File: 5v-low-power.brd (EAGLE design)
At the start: 68.6 x 40.3 mm, 34 parts, among them J1 Bypass, J2 En, J3 12v, J4 5V Out, J5 LED EN, J6 POWERPOLE_POWER10AWG, J7 POWERPOLE_POWER10AWG, Q1 SI4532ADY, U1 LT1934ES6TRMPBF

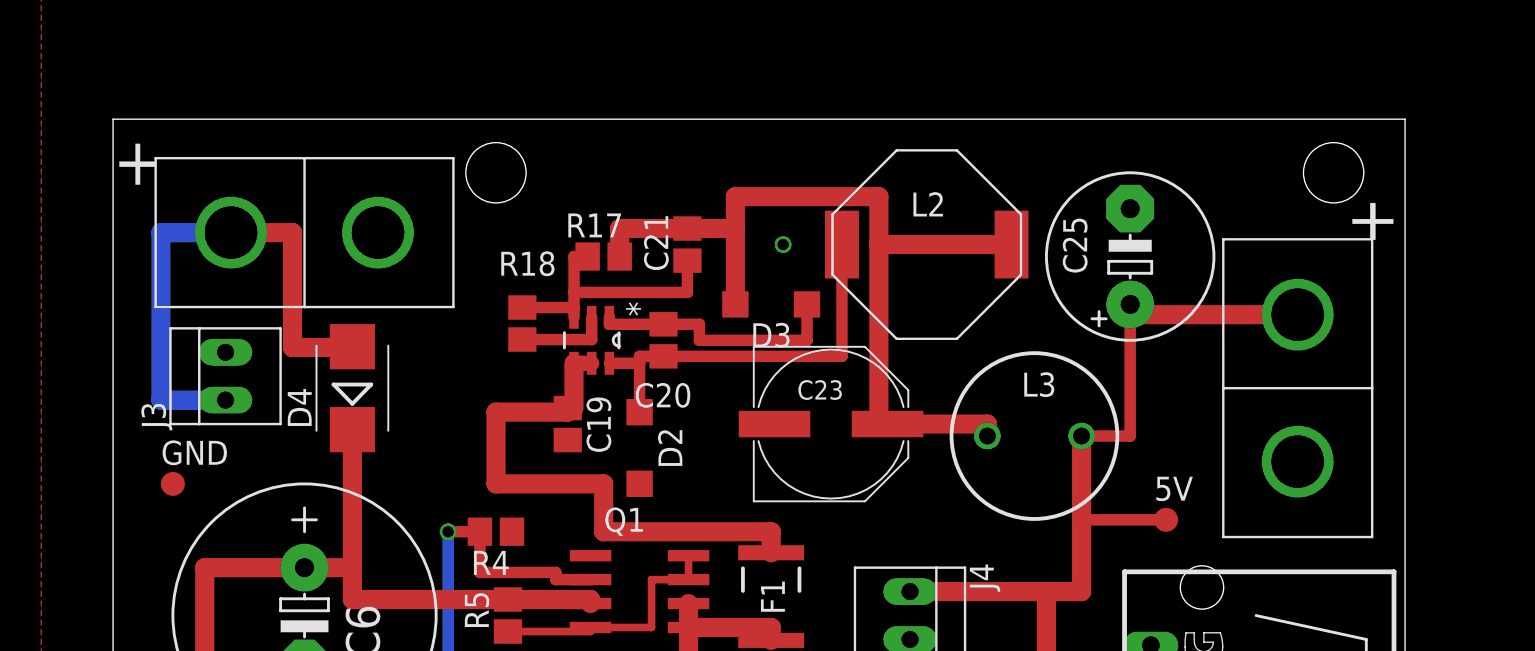
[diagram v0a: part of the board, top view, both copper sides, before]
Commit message: changed to correct powerpole version added current rating onto docu layer
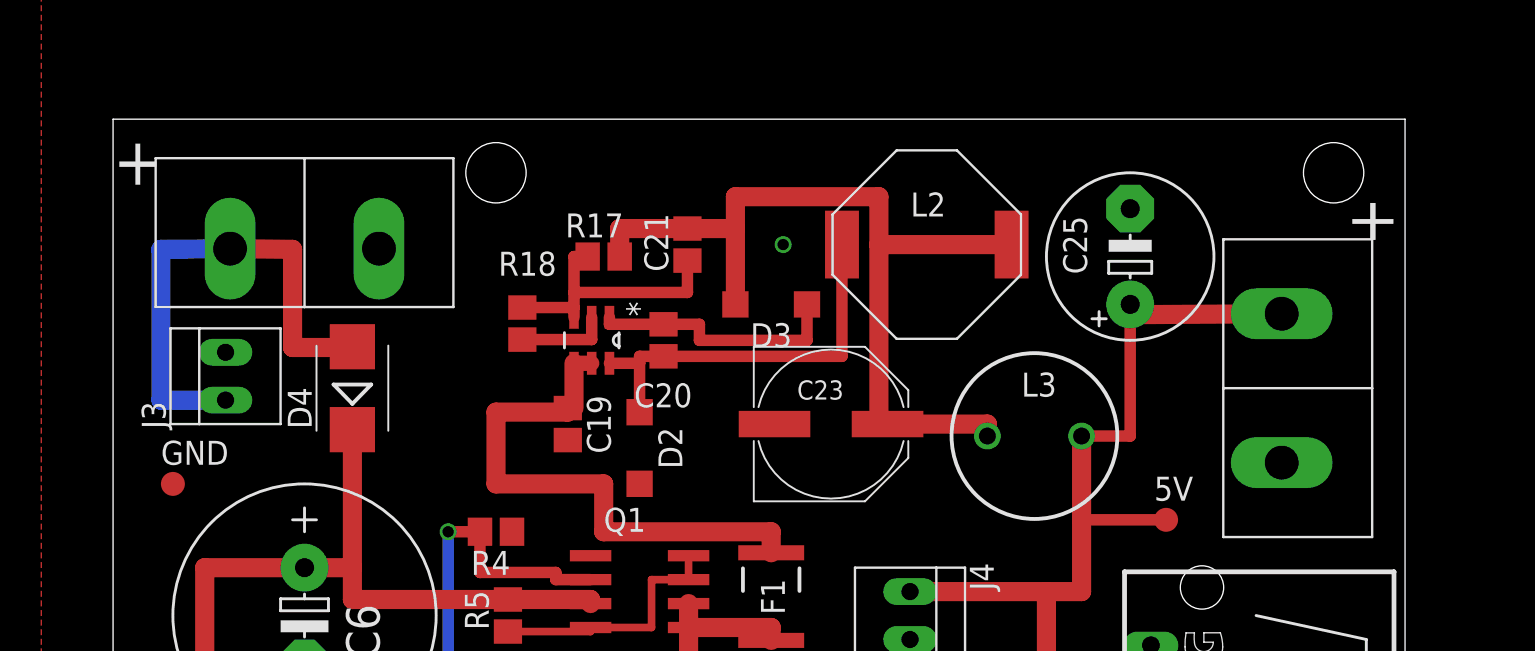
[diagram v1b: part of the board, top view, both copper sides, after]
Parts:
- J6, J7: value POWERPOLE_POWER10AWG -> POWERPOLE_POWER25A; device powerpoles:POWERPOLE_PAIR_10AWG -> powerpoles:POWERPOLE_PAIR_25A
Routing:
- net N$3: track 28.6 -> 26.8 mm
- net 5V: track 59.0 -> 58.1 mm
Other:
- board text added: "250mA"
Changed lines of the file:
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@@
 <text x="2.54" y="6.35" size="1.778" layer="51" rot="R90">V0.1</text>
 <text x="2.54" y="14.605" size="1.778" layer="51" rot="R90">PJB</text>
+<text x="53.975" y="38.1" size="1.778" layer="51">250mA</text>
 </plain>
 <attributes>
@@
 </element>
 <element name="J3" library="farnell-parts" package="2-MOLEX" value="12v" x="6.35" y="26.67" rot="R270"/>
-<element name="J6" library="powerpoles" package="POWERPOLE_PAIR_10AWG" value="POWERPOLE_POWER10AWG" x="62.865" y="26.035" rot="R270"/>
-<element name="J7" library="powerpoles" package="POWERPOLE_PAIR_10AWG" value="POWERPOLE_POWER10AWG" x="10.16" y="34.29"/>
+<element name="J6" library="powerpoles" package="POWERPOLE_PAIR_25A" value="POWERPOLE_POWER25A" x="62.865" y="26.035" rot="R270"/>
+<element name="J7" library="powerpoles" package="POWERPOLE_PAIR_25A" value="POWERPOLE_POWER25A" x="10.16" y="34.29"/>
 </elements>
 <signals>
@@
 <wire x1="51.395" y1="23.495" x2="53.975" y2="23.495" width="0.6096" layer="1"/>
 <wire x1="53.975" y1="23.495" x2="53.975" y2="30.48" width="0.6096" layer="1"/>
-<wire x1="62.865" y1="29.935" x2="53.975" y2="29.935" width="1.016" layer="1"/>
+<wire x1="62.015" y1="29.985" x2="53.975" y2="29.935" width="1.016" layer="1"/>
 <wire x1="53.975" y1="29.935" x2="53.975" y2="30.48" width="1.016" layer="1"/>
 <wire x1="42.291" y1="15.24" x2="49.53" y2="15.24" width="1.016" layer="1"/>
@@
 <contactref element="J7" pad="RED"/>
 <wire x1="5.969" y1="25.4" x2="2.54" y2="25.4" width="1.016" layer="16"/>
-<wire x1="2.54" y1="25.4" x2="2.54" y2="34.29" width="1.016" layer="16"/>
-<wire x1="2.54" y1="34.29" x2="6.26" y2="34.29" width="1.016" layer="16"/>
-<wire x1="6.26" y1="34.29" x2="9.525" y2="34.29" width="1.016" layer="1"/>
-<wire x1="9.525" y1="34.29" x2="9.525" y2="28.194" width="1.016" layer="1"/>
+<wire x1="2.54" y1="25.4" x2="2.54" y2="33.401" width="1.016" layer="16"/>
+<wire x1="2.54" y1="33.401" x2="6.21" y2="33.44" width="1.016" layer="16"/>
+<wire x1="6.21" y1="33.44" x2="9.525" y2="33.401" width="1.016" layer="1"/>
+<wire x1="9.525" y1="33.401" x2="9.525" y2="28.194" width="1.016" layer="1"/>
 <wire x1="9.525" y1="28.194" x2="12.7" y2="28.194" width="1.016" layer="1"/>
 <wire x1="12.7" y1="28.194" x2="12.7" y2="28.235" width="1.016" layer="1"/>

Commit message: Added additional USB footprints and rotated some powerpoles
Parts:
- removed X1: (no value), con-berg:PN87520
- added SJ1, SJ2, SJ3: (no value), jumper:SJ
- added U$1: USB_DUAL_VERT+HORIZTRIPPLE, power:USB_DUAL_HORIZ+VERT
- turned J6 to 90 degrees
- turned J7 to 180 degrees
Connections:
- new net N$2: SJ1.2, U$1.P1.3
- new net N$4: SJ1.1, U$1.P1.2
- new net N$5: SJ2.1, U$1.P2.2
- new net N$6: SJ2.2, U$1.P2.3
- new net N$7: SJ3.2, U$1.P3.3
- new net N$8: SJ3.1, U$1.P3.2
- net 5V: now also U$1.P1.1, U$1.P2.1, U$1.P3.1; no longer X1.1
- net GND: now also U$1.P1.4, U$1.P2.4, U$1.P3.4; no longer X1.4
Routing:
- net 5V: track 58.1 -> 76.2 mm
- net N$3: track 26.8 -> 17.9 mm
- net N$2: track 0.00 -> 3.41 mm
- net N$4: track 0.00 -> 3.41 mm
- net N$7: track 0.00 -> 2.62 mm
- net N$8: track 0.00 -> 2.62 mm
- net N$6: track 0.00 -> 2.39 mm
- net N$5: track 0.00 -> 2.39 mm
- net GND: vias 1 -> 2
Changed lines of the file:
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@@
 <?xml version="1.0" encoding="utf-8"?>
 <!DOCTYPE eagle SYSTEM "eagle.dtd">
-<eagle version="6.5.0">
+<eagle version="6.4">
 <drawing>
 <settings>
@@
 <setting verticaltext="up"/>
 </settings>
-<grid distance="25" unitdist="mil" unit="mm" style="lines" multiple="1" display="yes" altdistance="5" altunitdist="mil" altunit="mil"/>
+<grid distance="25" unitdist="mil" unit="mm" style="lines" multiple="1" display="yes" altdistance="5" altunitdist="mil" altunit="mm"/>
 <layers>
 <layer number="1" name="Top" color="4" fill="1" visible="yes" active="yes"/>
@@
 <wire x1="0" y1="40.31" x2="0" y2="0" width="0" layer="20"/>
 <hole x="64.77" y="37.465" drill="3.2"/>
-<hole x="20.32" y="37.465" drill="3.2"/>
+<hole x="21.59" y="37.465" drill="3.2"/>
 <hole x="3.175" y="3.175" drill="3.2"/>
-<text x="23.495" y="37.465" size="1.778" layer="51">5V Low Power</text>
+<text x="24.13" y="37.465" size="1.778" layer="51">5V Low Power</text>
 <text x="2.54" y="6.35" size="1.778" layer="51" rot="R90">V0.1</text>
 <text x="2.54" y="14.605" size="1.778" layer="51" rot="R90">PJB</text>
@@
 </element>
 <element name="D4" library="diode" package="SMB" value="" x="12.7" y="26.035" rot="R90"/>
-<element name="X1" library="con-berg" package="PN87520" value="" x="57.785" y="8.89" smashed="yes" rot="R90">
-<attribute name="OC_NEWARK" value="unknown" x="69.215" y="30.48" size="1.778" layer="27" rot="R90" display="off"/>
-<attribute name="MPN" value="" x="69.215" y="30.48" size="1.778" layer="27" rot="R90" display="off"/>
-<attribute name="MF" value="" x="69.215" y="30.48" size="1.778" layer="27" rot="R90" display="off"/>
-<attribute name="OC_FARNELL" value="unknown" x="69.215" y="30.48" size="1.778" layer="27" rot="R90" display="off"/>
-<attribute name="VALUE" x="67.945" y="18.034" size="1.27" layer="27" rot="R180"/>
-</element>
 <element name="GND" library="testpad" package="B1,27" value="5V B" x="3.175" y="20.955">
 <attribute name="TP_SIGNAL_NAME" value="" x="42.545" y="-48.895" size="1.778" layer="27" display="off"/>
 </element>
 <element name="J3" library="farnell-parts" package="2-MOLEX" value="12v" x="6.35" y="26.67" rot="R270"/>
-<element name="J6" library="powerpoles" package="POWERPOLE_PAIR_25A" value="POWERPOLE_POWER25A" x="62.865" y="26.035" rot="R270"/>
-<element name="J7" library="powerpoles" package="POWERPOLE_PAIR_25A" value="POWERPOLE_POWER25A" x="10.16" y="34.29"/>
+<element name="J6" library="powerpoles" package="POWERPOLE_PAIR_25A" value="POWERPOLE_POWER25A" x="62.865" y="26.035" rot="R90"/>
+<element name="J7" library="powerpoles" package="POWERPOLE_PAIR_25A" value="POWERPOLE_POWER25A" x="10.16" y="34.29" rot="R180"/>
+<element name="U$1" library="power" package="USB_DUAL_HORIZ+VERT" value="USB_DUAL_VERT+HORIZTRIPPLE" x="55.245" y="8.89" smashed="yes"/>
+<element name="SJ1" library="jumper" package="SJ" value="" x="58.42" y="8.89" rot="MR90"/>
+<element name="SJ2" library="jumper" package="SJ" value="" x="61.595" y="8.89" rot="MR90"/>
+<element name="SJ3" library="jumper" package="SJ" value="" x="50.165" y="8.89" rot="MR90"/>
 </elements>
 <signals>
@@
 <contactref element="J2" pad="1"/>
 <contactref element="J4" pad="1"/>
-<contactref element="X1" pad="4"/>
 <contactref element="J6" pad="BLACK"/>
 <contactref element="J5" pad="1"/>
@@
 <wire x1="25.4" y1="28.614" x2="25.4" y2="29.7942" width="0.6096" layer="1"/>
 <via x="35.56" y="33.655" extent="1-16" drill="0.6"/>
+<contactref element="U$1" pad="P1.4"/>
+<contactref element="U$1" pad="P2.4"/>
+<contactref element="U$1" pad="P3.4"/>
+<via x="60.96" y="2.54" extent="1-16" drill="0.6"/>
 </signal>
 <signal name="VCC">
@@
 <contactref element="5V" pad="TP"/>
 <contactref element="J4" pad="2"/>
-<contactref element="X1" pad="1"/>
 <contactref element="J6" pad="RED"/>
 <wire x1="51.395" y1="23.495" x2="53.975" y2="23.495" width="0.6096" layer="1"/>
-<wire x1="53.975" y1="23.495" x2="53.975" y2="30.48" width="0.6096" layer="1"/>
-<wire x1="62.015" y1="29.985" x2="53.975" y2="29.935" width="1.016" layer="1"/>
+<wire x1="53.975" y1="23.495" x2="53.975" y2="29.935" width="0.6096" layer="1"/>
 <wire x1="53.975" y1="29.935" x2="53.975" y2="30.48" width="1.016" layer="1"/>
-<wire x1="42.291" y1="15.24" x2="49.53" y2="15.24" width="1.016" layer="1"/>
-<wire x1="49.53" y1="15.24" x2="51.395" y2="15.24" width="1.016" layer="1"/>
-<wire x1="51.395" y1="15.24" x2="51.395" y2="19.05" width="1.016" layer="1"/>
+<wire x1="42.291" y1="15.24" x2="42.545" y2="15.24" width="1.016" layer="1"/>
+<wire x1="42.545" y1="15.24" x2="42.505" y2="19.05" width="1.016" layer="1"/>
+<wire x1="42.505" y1="19.05" x2="51.395" y2="19.05" width="1.016" layer="1"/>
 <wire x1="51.395" y1="19.05" x2="51.395" y2="23.495" width="1.016" layer="1"/>
-<wire x1="55.075" y1="5.39" x2="49.53" y2="5.39" width="1.016" layer="1"/>
-<wire x1="49.53" y1="5.39" x2="49.53" y2="9.525" width="1.016" layer="1"/>
-<wire x1="49.53" y1="9.525" x2="49.53" y2="15.24" width="1.016" layer="1"/>
-<wire x1="46.99" y1="9.74" x2="49.53" y2="9.74" width="0.6096" layer="1"/>
+<wire x1="46.99" y1="9.74" x2="49.53" y2="9.74" width="0.8128" layer="1"/>
 <wire x1="49.53" y1="9.74" x2="49.53" y2="9.525" width="0.6096" layer="1"/>
 <wire x1="55.88" y1="19.05" x2="51.395" y2="19.05" width="0.6096" layer="1"/>
+<contactref element="U$1" pad="P1.1"/>
+<contactref element="U$1" pad="P2.1"/>
+<contactref element="U$1" pad="P3.1"/>
+<wire x1="42.545" y1="15.24" x2="46.99" y2="15.24" width="0.8128" layer="1"/>
+<wire x1="46.99" y1="15.24" x2="46.99" y2="9.74" width="0.8128" layer="1"/>
+<wire x1="63.745" y1="5.39" x2="55.245" y2="5.39" width="0.8128" layer="1"/>
+<wire x1="55.245" y1="5.39" x2="52.545" y2="5.39" width="0.8128" layer="1"/>
+<wire x1="52.545" y1="5.39" x2="49.53" y2="5.39" width="0.8128" layer="1"/>
+<wire x1="49.53" y1="5.39" x2="49.53" y2="9.525" width="0.8128" layer="1"/>
+<wire x1="63.715" y1="22.085" x2="51.395" y2="22.085" width="1.016" layer="1"/>
+<wire x1="51.395" y1="22.085" x2="51.395" y2="23.495" width="0.8128" layer="1"/>
 </signal>
 <signal name="LEDGND1">
@@
 <contactref element="D4" pad="A"/>
 <contactref element="J7" pad="RED"/>
-<wire x1="5.969" y1="25.4" x2="2.54" y2="25.4" width="1.016" layer="16"/>
-<wire x1="2.54" y1="25.4" x2="2.54" y2="33.401" width="1.016" layer="16"/>
-<wire x1="2.54" y1="33.401" x2="6.21" y2="33.44" width="1.016" layer="16"/>
-<wire x1="6.21" y1="33.44" x2="9.525" y2="33.401" width="1.016" layer="1"/>
-<wire x1="9.525" y1="33.401" x2="9.525" y2="28.194" width="1.016" layer="1"/>
 <wire x1="9.525" y1="28.194" x2="12.7" y2="28.194" width="1.016" layer="1"/>
 <wire x1="12.7" y1="28.194" x2="12.7" y2="28.235" width="1.016" layer="1"/>
+<wire x1="12.7" y1="28.235" x2="14.11" y2="28.235" width="1.016" layer="1"/>
+<wire x1="14.11" y1="28.235" x2="14.11" y2="35.14" width="1.016" layer="1"/>
+<wire x1="9.525" y1="28.194" x2="9.525" y2="25.4" width="1.016" layer="1"/>
+<wire x1="9.525" y1="25.4" x2="5.969" y2="25.4" width="1.016" layer="1"/>
+</signal>
+<signal name="N$2">
+<contactref element="SJ1" pad="2"/>
+<contactref element="U$1" pad="P1.3"/>
+<wire x1="58.42" y1="9.652" x2="55.245" y2="9.652" width="0.4064" layer="16"/>
+<wire x1="55.245" y1="9.652" x2="55.245" y2="9.89" width="0.4064" layer="16"/>
+</signal>
+<signal name="N$4">
+<contactref element="U$1" pad="P1.2"/>
+<contactref element="SJ1" pad="1"/>
+<wire x1="58.42" y1="8.128" x2="55.245" y2="8.128" width="0.4064" layer="16"/>
+<wire x1="55.245" y1="8.128" x2="55.245" y2="7.89" width="0.4064" layer="16"/>
+</signal>
+<signal name="N$5">
+<contactref element="SJ2" pad="1"/>
+<contactref element="U$1" pad="P2.2"/>
+<wire x1="61.595" y1="8.128" x2="63.745" y2="8.128" width="0.4064" layer="16"/>
+<wire x1="63.745" y1="8.128" x2="63.745" y2="7.89" width="0.4064" layer="16"/>
+</signal>
+<signal name="N$6">
+<contactref element="SJ2" pad="2"/>
+<contactref element="U$1" pad="P2.3"/>
+<wire x1="61.595" y1="9.652" x2="63.745" y2="9.652" width="0.4064" layer="16"/>
+<wire x1="63.745" y1="9.652" x2="63.745" y2="9.89" width="0.4064" layer="16"/>
+</signal>
+<signal name="N$7">
+<contactref element="SJ3" pad="2"/>
+<contactref element="U$1" pad="P3.3"/>
+<wire x1="50.165" y1="9.652" x2="52.545" y2="9.652" width="0.4064" layer="16"/>
+<wire x1="52.545" y1="9.652" x2="52.545" y2="9.89" width="0.4064" layer="16"/>
+</signal>
+<signal name="N$8">
+<contactref element="SJ3" pad="1"/>
+<contactref element="U$1" pad="P3.2"/>
+<wire x1="50.165" y1="8.128" x2="52.545" y2="8.128" width="0.4064" layer="16"/>
+<wire x1="52.545" y1="8.128" x2="52.545" y2="7.89" width="0.4064" layer="16"/>
 </signal>
 </signals>
